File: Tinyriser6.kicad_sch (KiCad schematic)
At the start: 21 parts, among them J1 Bus_M.2_Socket_M, J2 Bus_PCI_Express_x16, J3 Conn_02x04_Odd_Even, J6 USB_A, J7 Conn_02x10_Odd_Even, M1 Fan_4pin

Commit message: changed usb footprint
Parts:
- J6: footprint Connector_USB:USB_A_Wuerth_614004134726_Horizontal -> A-my-stuff:USB-A-TH_HC-USB2.0-L100-W; part url (none) -> https://www.lcsc.com/product-detail/USB-Connectors_Hong-Che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

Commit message: working on changing misc io header to 2.54mm and set m.2 slot to thermal reliefs for handsoldering
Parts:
- J7: footprint Connector_PinHeader_2.00mm:PinHeader_2x10_P2.00mm_Vertical -> Connector_PinHeader_2.54mm:PinHeader_2x10_P2.54mm_Vertical

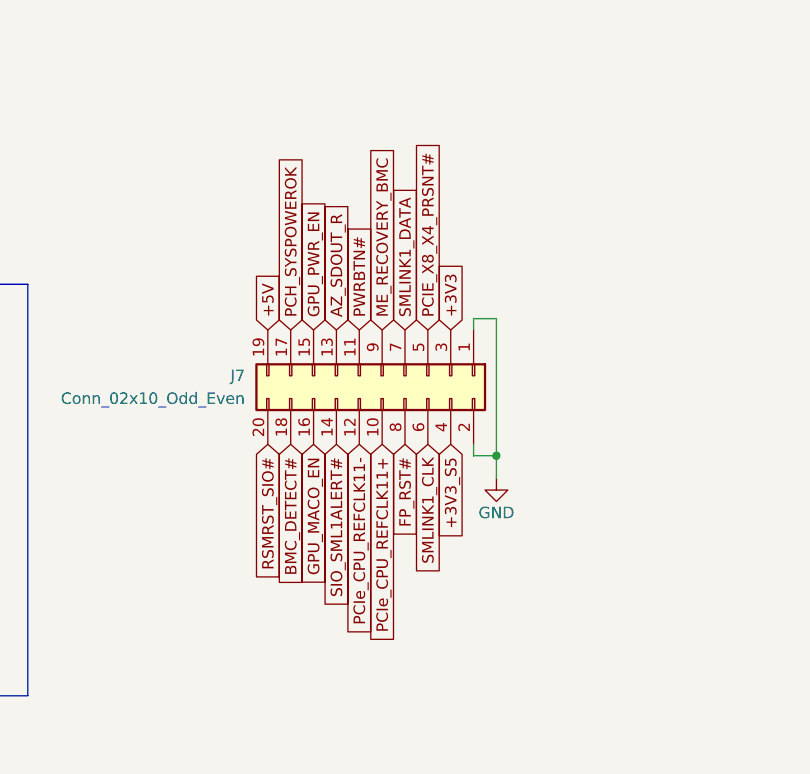
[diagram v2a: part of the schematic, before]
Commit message: Finished changing misc io header to 2.54mm?
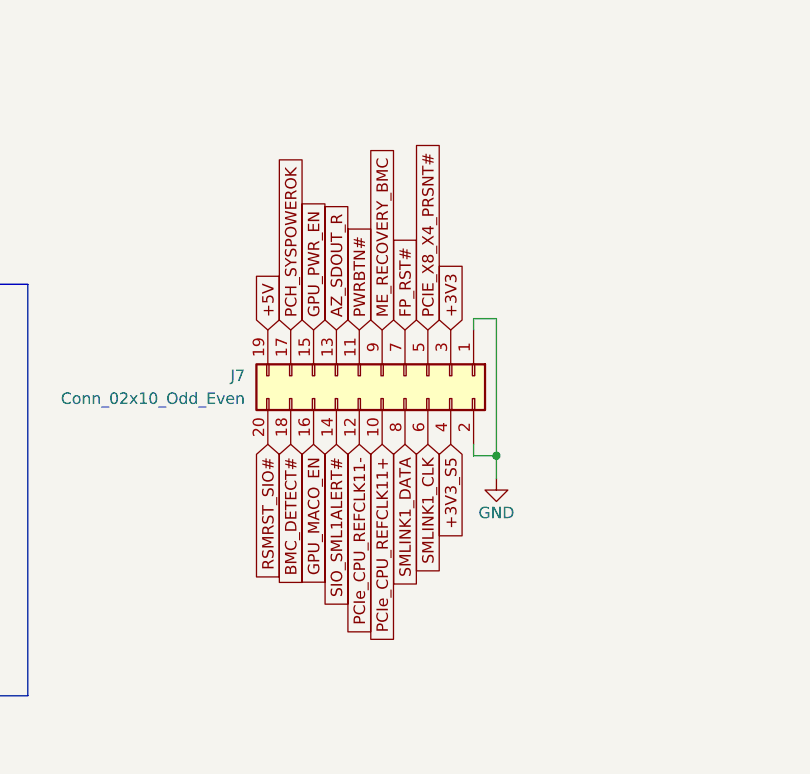
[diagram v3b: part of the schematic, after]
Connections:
- net FP_RST#: now also J7.7 (Pin_7); no longer J7.8 (Pin_8)
- net SMLINK1_DATA: now also J7.8 (Pin_8); no longer J7.7 (Pin_7)

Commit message: Finalized USB port
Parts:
- J6: footprint A-my-stuff:USB-A-TH_HC-USB2.0-L100-W -> A-my-stuff:that-sideways-usb; part url https://www.lcsc.com/product-detail/USB-Connectors_Hong-Che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 -> https://www.lcsc.com/product-detail/USB-Connectors_Jing-Ext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

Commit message: bunch of minor changes
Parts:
- renumbered J4 to J1, J1 to J3, J3 to J4, J6 to J5, J7 to J6, J5 to J7

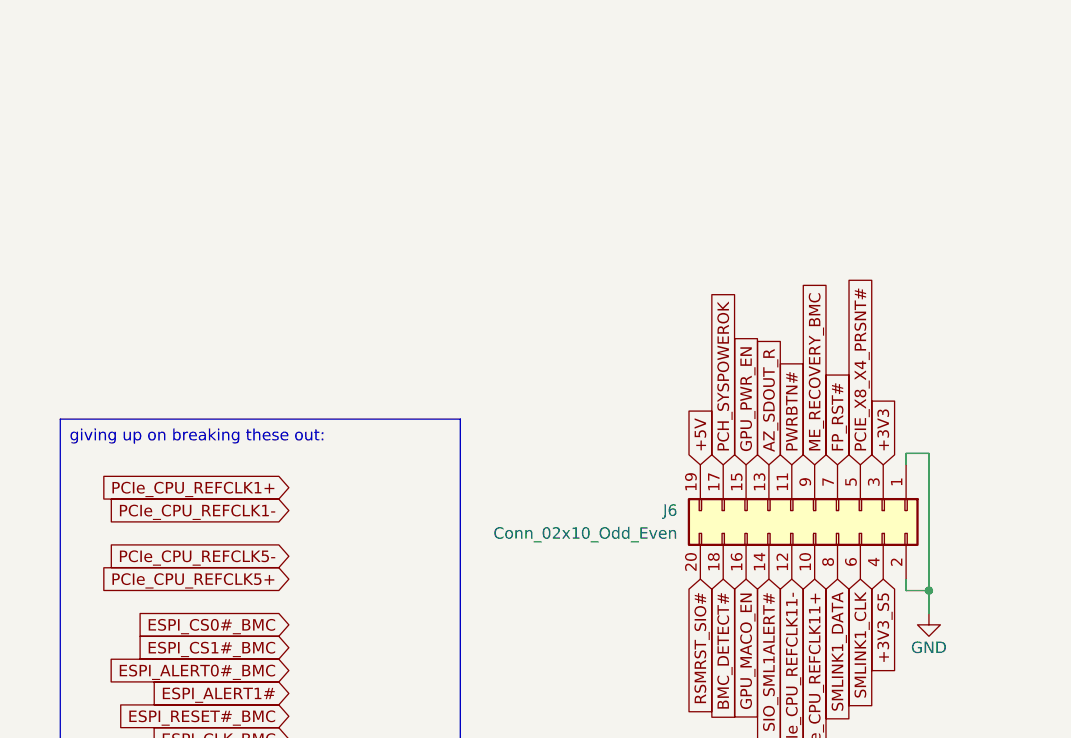
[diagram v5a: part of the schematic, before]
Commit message: Changed misc io header pin numbering and added labels for pinout
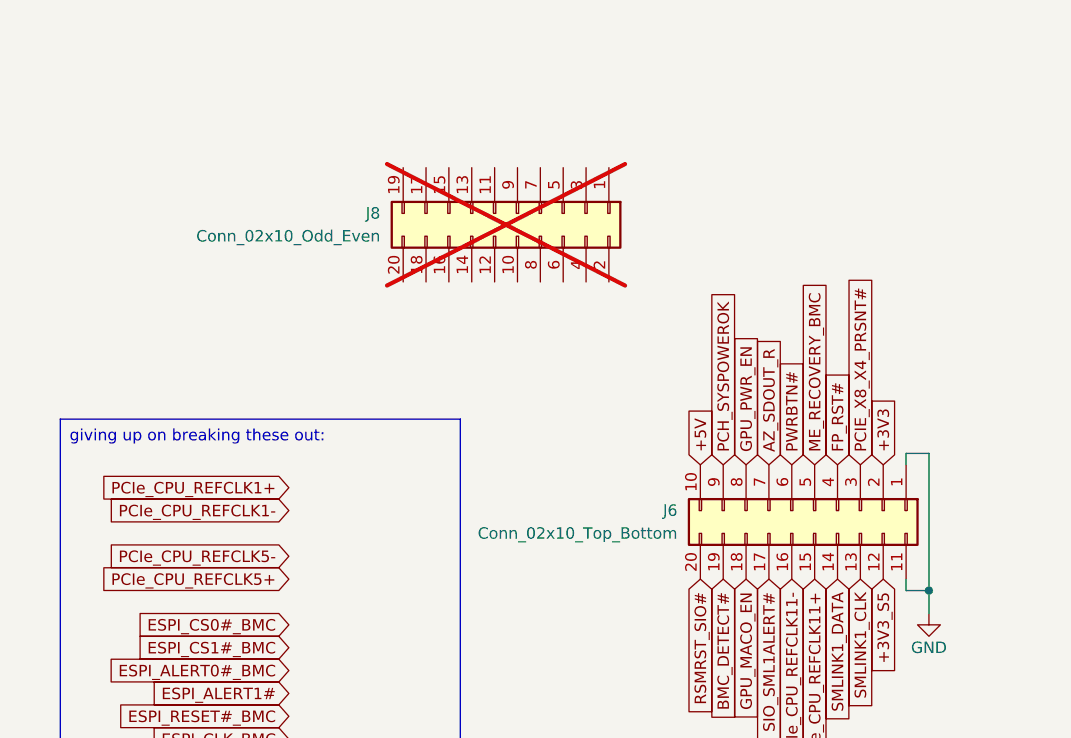
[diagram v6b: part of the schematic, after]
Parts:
- added J6: Conn_02x10_Top_Bottom, Connector_PinHeader_2.54mm:PinHeader_2x10_P2.54mm_Vertical, symbol Connector_Generic:Conn_02x10_Top_Bottom
- J8: renamed from J6; now not fitted
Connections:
- net +3V3: now also J6.2 (Pin_2); no longer J8.3 (Pin_3)
- net +3V3_S5: now also J6.12 (Pin_12); no longer J8.4 (Pin_4)
- net +5V: now also J6.10 (Pin_10); no longer J8.19 (Pin_19)
- net AZ_SDOUT_R: now also J6.7 (Pin_7); no longer J8.13 (Pin_13)
- net BMC_DETECT#: now also J6.19 (Pin_19); no longer J8.18 (Pin_18)
- net FP_RST#: now also J6.4 (Pin_4); no longer J8.7 (Pin_7)
- net GND: now also J6.1 (Pin_1), J6.11 (Pin_11); no longer J8.1 (Pin_1), J8.2 (Pin_2)
- net GPU_MACO_EN: now also J6.18 (Pin_18); no longer J8.16 (Pin_16)
- net GPU_PWR_EN: now also J6.8 (Pin_8); no longer J8.15 (Pin_15)
- net ME_RECOVERY_BMC: now also J6.5 (Pin_5); no longer J8.9 (Pin_9)
- net PCH_SYSPOWEROK: now also J6.9 (Pin_9); no longer J8.17 (Pin_17)
- net PCIE_X8_X4_PRSNT#: now also J6.3 (Pin_3); no longer J8.5 (Pin_5)
- net PCIe_CPU_REFCLK11+: now also J6.15 (Pin_15); no longer J8.10 (Pin_10)
- net PCIe_CPU_REFCLK11-: now also J6.16 (Pin_16); no longer J8.12 (Pin_12)
- net PWRBTN#: now also J6.6 (Pin_6); no longer J8.11 (Pin_11)
- net RSMRST_SIO#: now also J6.20 (Pin_20); no longer J8.20 (Pin_20)
- net SIO_SML1ALERT#: now also J6.17 (Pin_17); no longer J8.14 (Pin_14)
- net SMLINK1_CLK: now also J6.13 (Pin_13); no longer J8.6 (Pin_6)
- net SMLINK1_DATA: now also J6.14 (Pin_14); no longer J8.8 (Pin_8)

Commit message: didn't label my schematic sheet right smh 😔
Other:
- title: TinyRiser v1 -> TinyRiser6 v1
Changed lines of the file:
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@@
 	(paper "A3")
 	(title_block
-		(title "TinyRiser v1")
+		(title "TinyRiser6 v1")
 		(rev "meow")
 		(company "WifiCable")

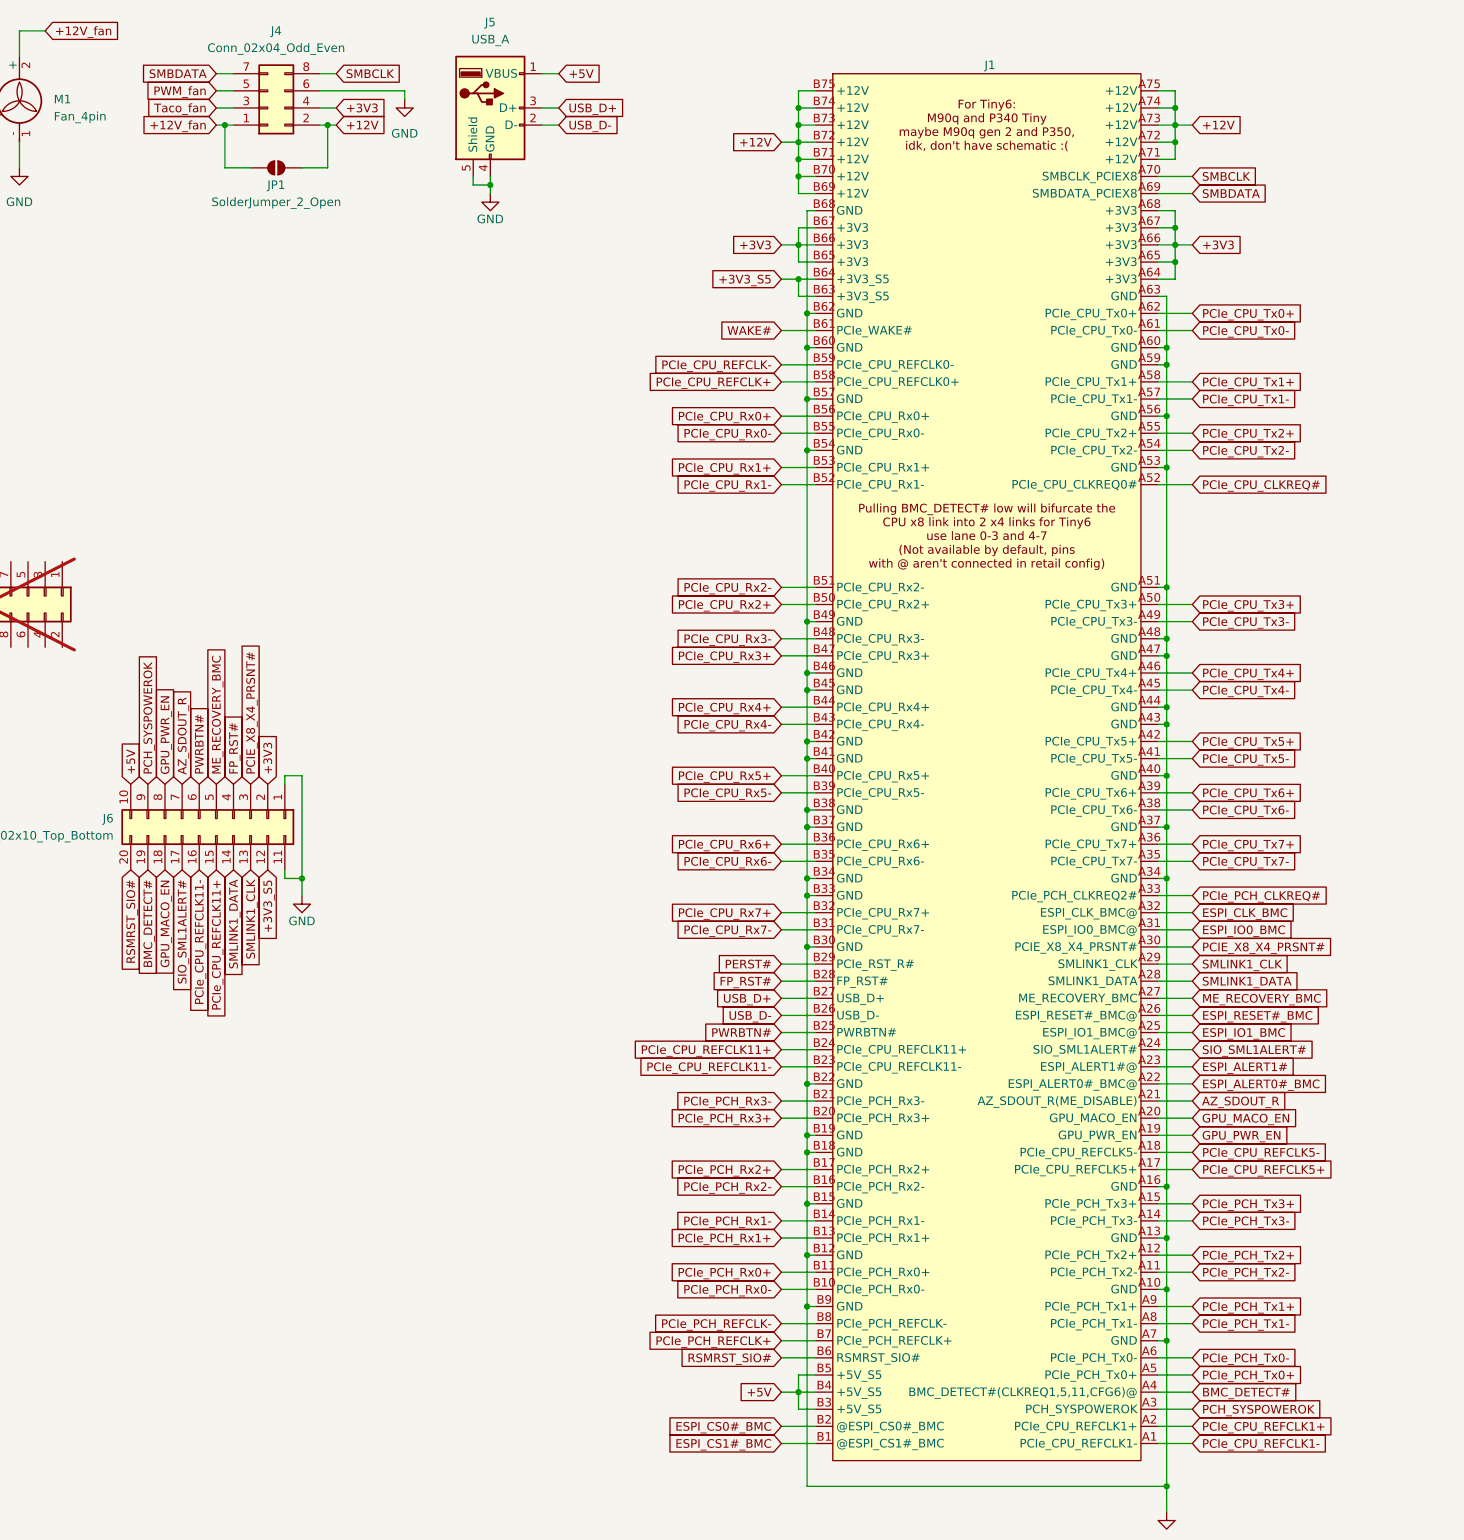
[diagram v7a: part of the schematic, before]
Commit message: Fixed some net names
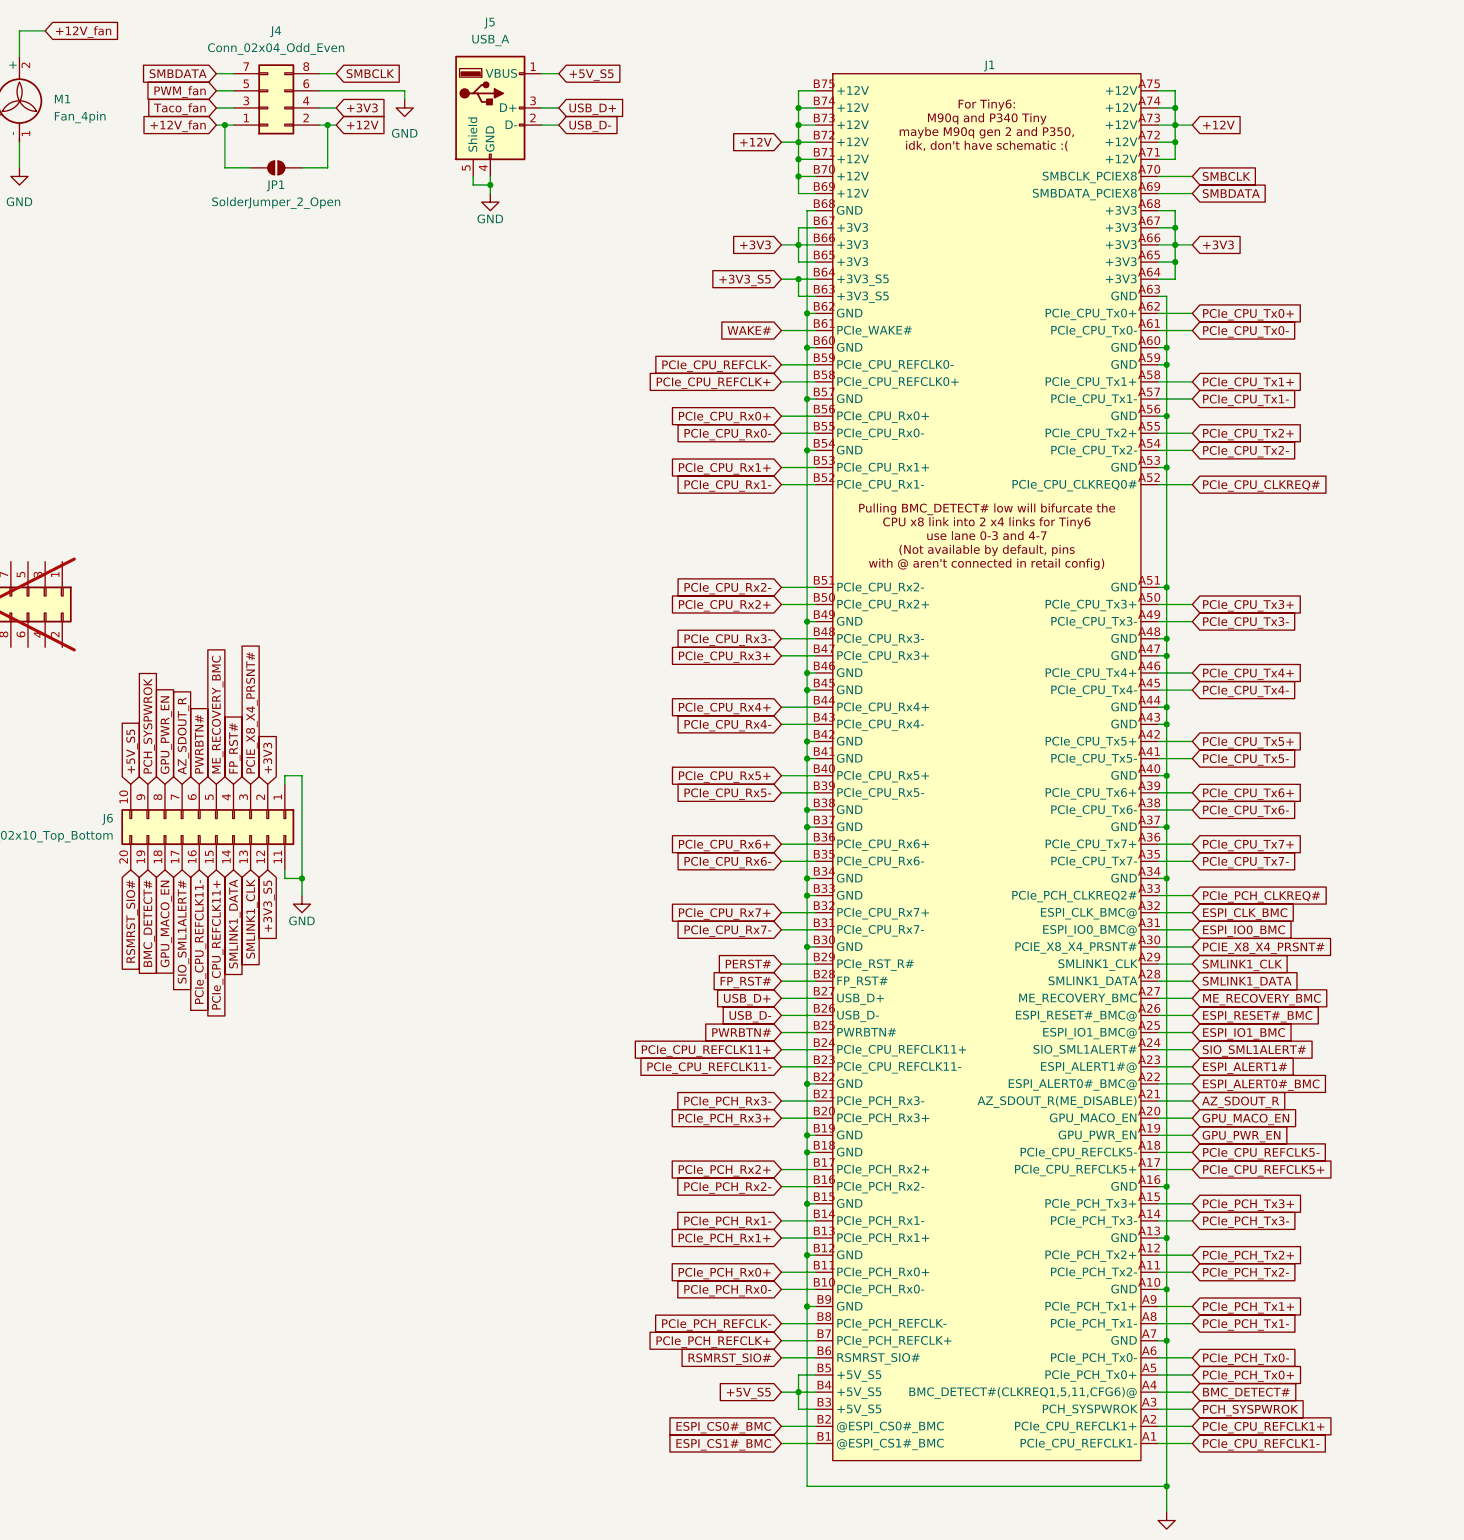
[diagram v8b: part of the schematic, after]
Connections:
- net +5V renamed +5V_S5
- net PCH_SYSPOWEROK renamed PCH_SYSPWROK
